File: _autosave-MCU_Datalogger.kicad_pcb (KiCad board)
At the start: 2 copper layers, 53 x 32.6 mm, 29 parts, among them J1 Conn_01x04_Pin, J2 Conn_01x04_Pin, J3 Conn_01x09_Pin, J4 Conn_02x03_Odd_Even, U1 24LC1025, U2 24LC1025, U3 DS1337S_, U4 ATMEGA328P-AU, Y1 32.768 KHz, Y2 16 MHz

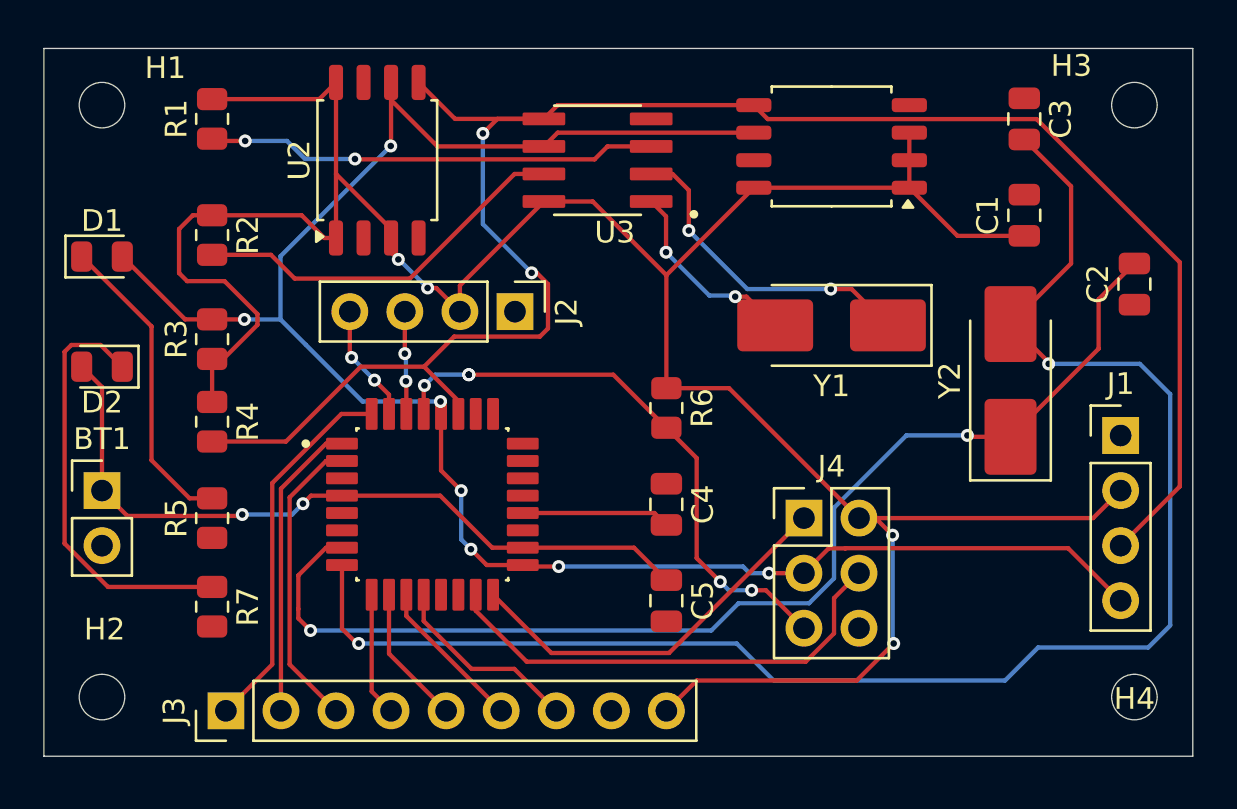
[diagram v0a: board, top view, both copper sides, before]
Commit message: Added proper Routing plus GND
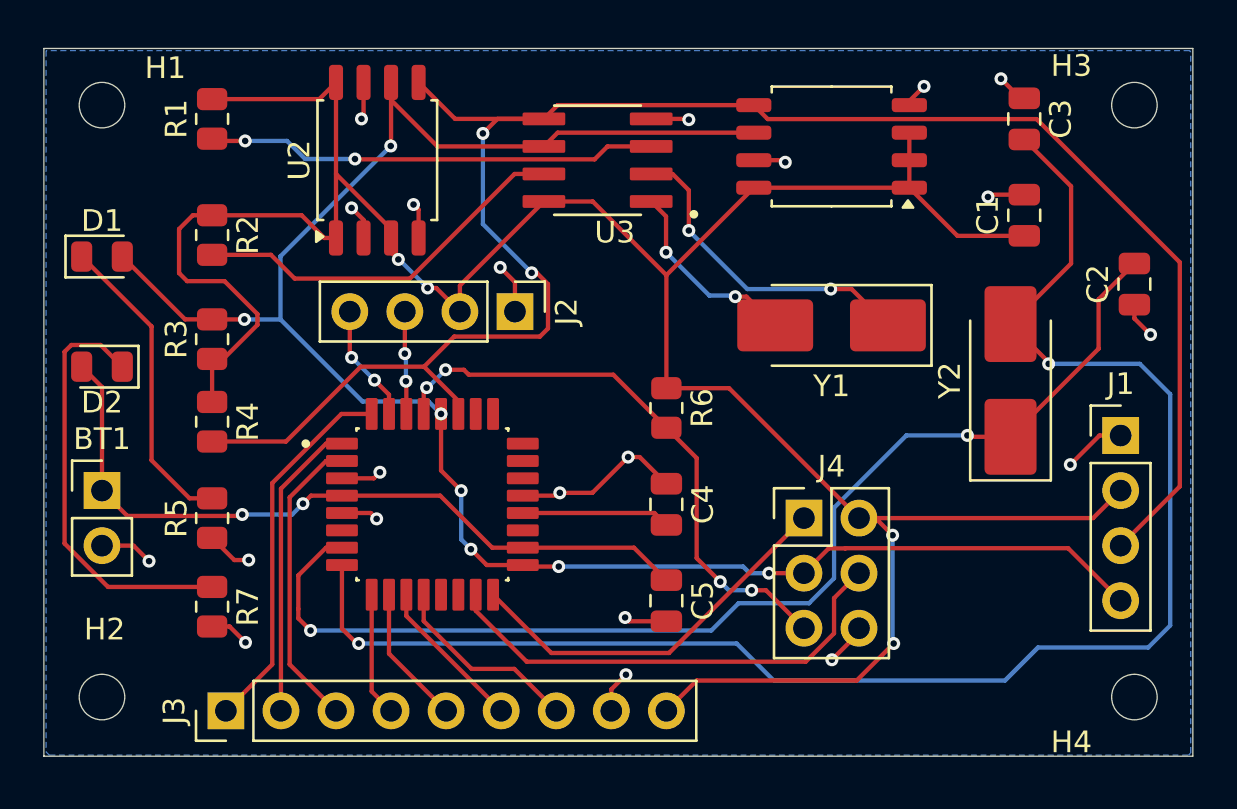
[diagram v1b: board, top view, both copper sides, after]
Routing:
- net GND: track 0.00 -> 43.2 mm, vias 0 -> 21
- net /RESET: track 26.6 -> 26.7 mm, vias 5 -> 4
- added copper zone on B.Cu, net GND
